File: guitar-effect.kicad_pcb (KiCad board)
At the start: 2 copper layers, 86.4 x 56.5 mm, 54 parts, among them IC1 PCM3002E, IC4 MCP6007-E_SN, IC5 MCP6007-E_SN, J1 Barrel_Jack_Switch, J2 Conn_01x11_Pin, J3 Conn_01x08_Pin, J4 NRJ4HF, J5 NRJ4HF, U1 LD1117S12TR_SOT223, U2 LD1117S33TR_SOT223

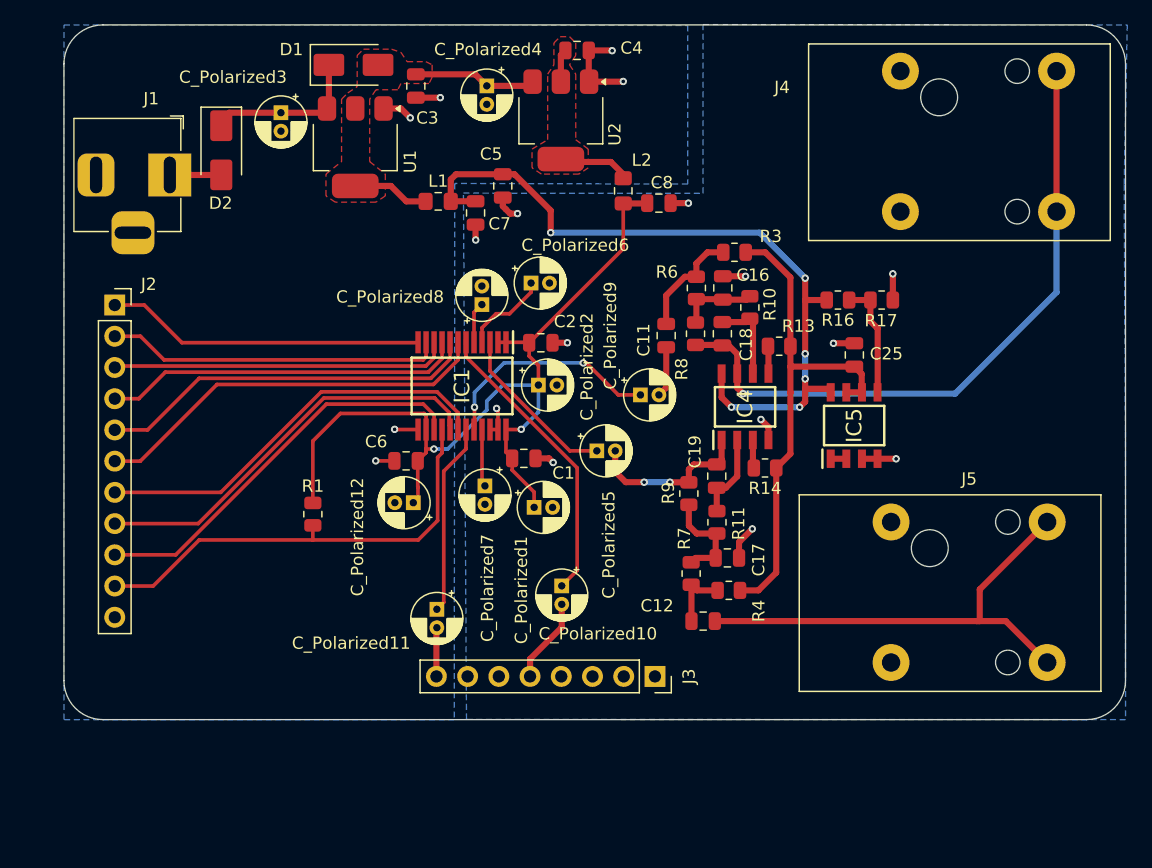
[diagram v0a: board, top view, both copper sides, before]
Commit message: PCB v1.2
Connecting the digital and analogue ground. Analogue parts are put farther away from the digital parts, on the right side of the PCB.
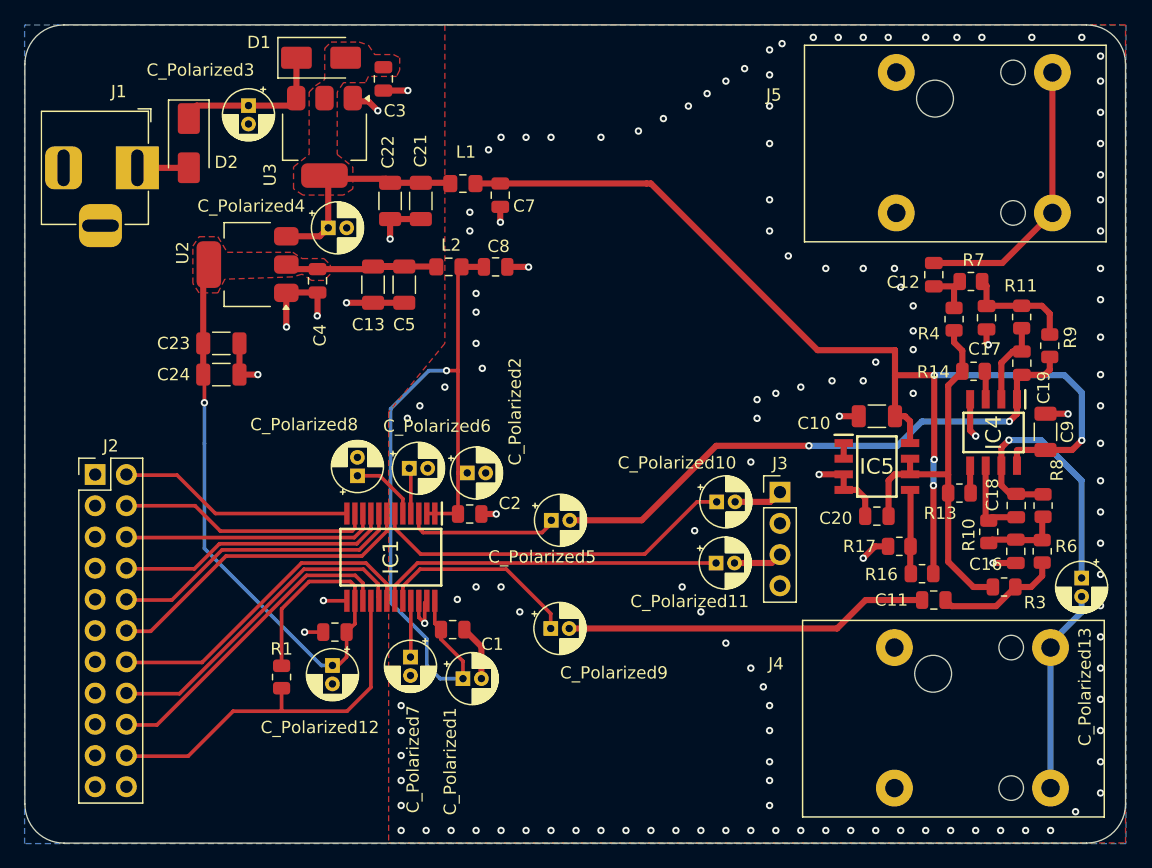
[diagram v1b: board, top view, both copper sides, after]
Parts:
- removed C25: 100n, Capacitor_SMD:C_0805_2012Metric
- removed U1: LD1117S12TR_SOT223, Package_TO_SOT_SMD:SOT-223-3_TabPin2
- added C10: 10u, Capacitor_SMD:C_1206_3216Metric, F.Cu at (193.1, 95.3)
- added C13: 10u, Capacitor_SMD:C_1206_3216Metric, F.Cu at (152.1, 84.6)
- added C20: 100n, Capacitor_SMD:C_0805_2012Metric, F.Cu at (193.1, 103.5)
- added C21: 10u, Capacitor_SMD:C_1206_3216Metric, F.Cu at (156.0, 77.8)
- added C22: 10u, Capacitor_SMD:C_1206_3216Metric, F.Cu at (153.5, 77.8)
- added C23: 10u, Capacitor_SMD:C_1206_3216Metric, F.Cu at (139.8, 89.4)
- added C24: 10u, Capacitor_SMD:C_1206_3216Metric, F.Cu at (139.8, 91.9)
- added C9: 10u, Capacitor_SMD:C_1206_3216Metric, F.Cu at (206.8, 96.6)
- added C_Polarized13: 870u, Capacitor_THT:CP_Radial_D4.0mm_P1.50mm, F.Cu at (209.8, 108.5)
- added U3: LD1117S50TR_SOT223, Package_TO_SOT_SMD:SOT-223-3_TabPin2, F.Cu at (148.2, 72.6)
- C11, C12: value 1u -> 22u
- C16, C17: value 1.5n -> 10n
- C18, C19: value 560p -> 1n
- C5: value 100n -> 10u; footprint Capacitor_SMD:C_0805_2012Metric -> Capacitor_SMD:C_1206_3216Metric
- J2: value Conn_01x11_Pin -> Conn_02x11_Odd_Even; footprint Connector_PinSocket_2.54mm:PinSocket_1x11_P2.54mm_Vertical -> Connector_PinHeader_2.54mm:PinHeader_2x11_P2.54mm_Vertical
- J3: value Conn_01x08_Pin -> Conn_01x04_Pin; footprint Connector_PinSocket_2.54mm:PinSocket_1x08_P2.54mm_Vertical -> Connector_PinHeader_2.54mm:PinHeader_1x04_P2.54mm_Vertical
- R10, R11: value 2k -> 1.5k
- R6, R7: value 3.3k -> 1.5k
- R8, R9: value 1.6k -> 3k
- moved J4 46.9 mm to (194.6, 114.2)
- moved J5 36.6 mm to (194.7, 67.4)
- moved R6 35.4 mm to (206.6, 106.3), turned to 90 degrees
- moved R3 35.0 mm to (203.5, 109.2), turned to 180 degrees
- moved C12 33.9 mm to (197.8, 83.8), turned to 90 degrees
- moved R7 32.9 mm to (200.8, 84.4), turned to 0 degrees
- moved C16 32.0 mm to (204.4, 106.3), turned to 90 degrees
- moved R9 31.7 mm to (207.2, 89.6), turned to 90 degrees
- moved R8 31.5 mm to (206.7, 102.6), turned to -90 degrees
- moved C11 30.6 mm to (197.8, 110.3), turned to 180 degrees
- moved R11 29.9 mm to (204.9, 87.3), turned to -90 degrees
- moved C17 28.7 mm to (202.1, 87.3), turned to 90 degrees
- moved R4 28.7 mm to (199.4, 87.4), turned to -90 degrees
- moved C4 28.2 mm to (147.6, 84.3), turned to -90 degrees
- moved U2 28.1 mm to (141.9, 83.0), turned to 180 degrees
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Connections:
- C18 pad 2: GUITAR_OUT -> Net-(IC4-VOUT_B)
- C3 pad 2: GND -> AGND
- C4 pad 2: GND -> AGND
- C5 pad 1: AVCC -> VDD
- C6 pad 1: AVDD -> VDD
- C6 pad 2: GND -> AGND
- C_Polarized12 pad 1: AVDD -> VDD
- C_Polarized12 pad 2: GND -> AGND
- C_Polarized3 pad 2: GND -> AGND
- C_Polarized4 pad 2: GND -> AGND
- IC1 pad 13: GND -> AGND
- IC1 pad 14: AVDD -> VDD
- IC4 pad 7: GUITAR_OUT -> Net-(IC4-VOUT_B)
- J1 pad 2: GND -> AGND
- J1 pad 3: GND -> AGND
- J2 pad 1: DATA_OUT -> AGND
- J2 pad 10: ZFLG -> ML/PDDA
- J2 pad 11: GND -> AGND
- J2 pad 2: BIT -> DATA_OUT
- J2 pad 3: LRCLK -> AGND
- J2 pad 4: SYSCLK -> BIT
- J2 pad 5: ML/PDDA -> AGND
- J2 pad 6: RST/PDAD -> LRCLK
- J2 pad 7: MC/DEM0 -> AGND
- J2 pad 8: MC/DEM1 -> SYSCLK
- J2 pad 9: DIN -> AGND
- J3 pad 1: unconnected-(J3-Pin_1-Pad1) -> LCH_IN
- J3 pad 3: AGND -> LCH_OUT
- J3 pad 4: unconnected-(J3-Pin_4-Pad4) -> AGND
- R1 pad 2: AVDD -> VDD
- R8 pad 1: GUITAR_OUT -> Net-(IC4-VOUT_B)
- U2 pad 1: GND -> AGND
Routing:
- net VDD: track 8.60 -> 71.8 mm, vias 0 -> 1
- net GUITAR_OUT: track 54.0 -> 16.6 mm, vias 1 -> 0
- net AGND: track 23.3 -> 59.7 mm, vias 12 -> 145
- net RCH_IN: track 13.7 -> 46.8 mm
- net AVCC: track 60.6 -> 91.0 mm, vias 6 -> 4
- net RCH_OUT: track 4.13 -> 29.7 mm
- net Net-(IC4-VOUT_B): track 0.00 -> 22.8 mm, vias 0 -> 1
- net GUITAR_IN: track 39.0 -> 22.8 mm
- net GND: track 15.2 -> 0.00 mm, vias 6 -> 0
- net Net-(IC1-VOUTL): track 15.6 -> 28.1 mm
- net VGND: track 41.4 -> 33.3 mm
- net MC/DEM1: track 33.3 -> 26.5 mm
- net RST/PDAD: track 32.8 -> 25.9 mm
- net MC/DEM0: track 33.4 -> 26.5 mm
- net SYSCLK: track 29.3 -> 22.5 mm
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- added copper zone on F.Cu, net AGND
- removed copper zone on B.Cu, net GND
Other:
- board size 86.4 x 56.5 mm -> 89.5 x 66.6 mm

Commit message: Forrasztáshoz
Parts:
- added D3: LED, LED_SMD:LED_0805_2012Metric_Pad1.15x1.40mm_HandSolder, F.Cu at (157.4, 67.0)
- added R2: 1k5, Resistor_SMD:R_0805_2012Metric_Pad1.20x1.40mm_HandSolder, F.Cu at (158.4, 70.1)
- C13, C21, C22, C23, C24, C5: value 10u -> 150u
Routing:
- net VCC: track 18.4 -> 21.8 mm
- net Net-(D3-K): track 0.00 -> 2.12 mm
- net AGND: track 59.7 -> 61.2 mm, vias 145 -> 160
